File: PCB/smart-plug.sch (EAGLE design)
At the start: 15 parts, among them K1 HLS8L-DC3V-S-C, T1 2N2222, X3 OUT-3PINS

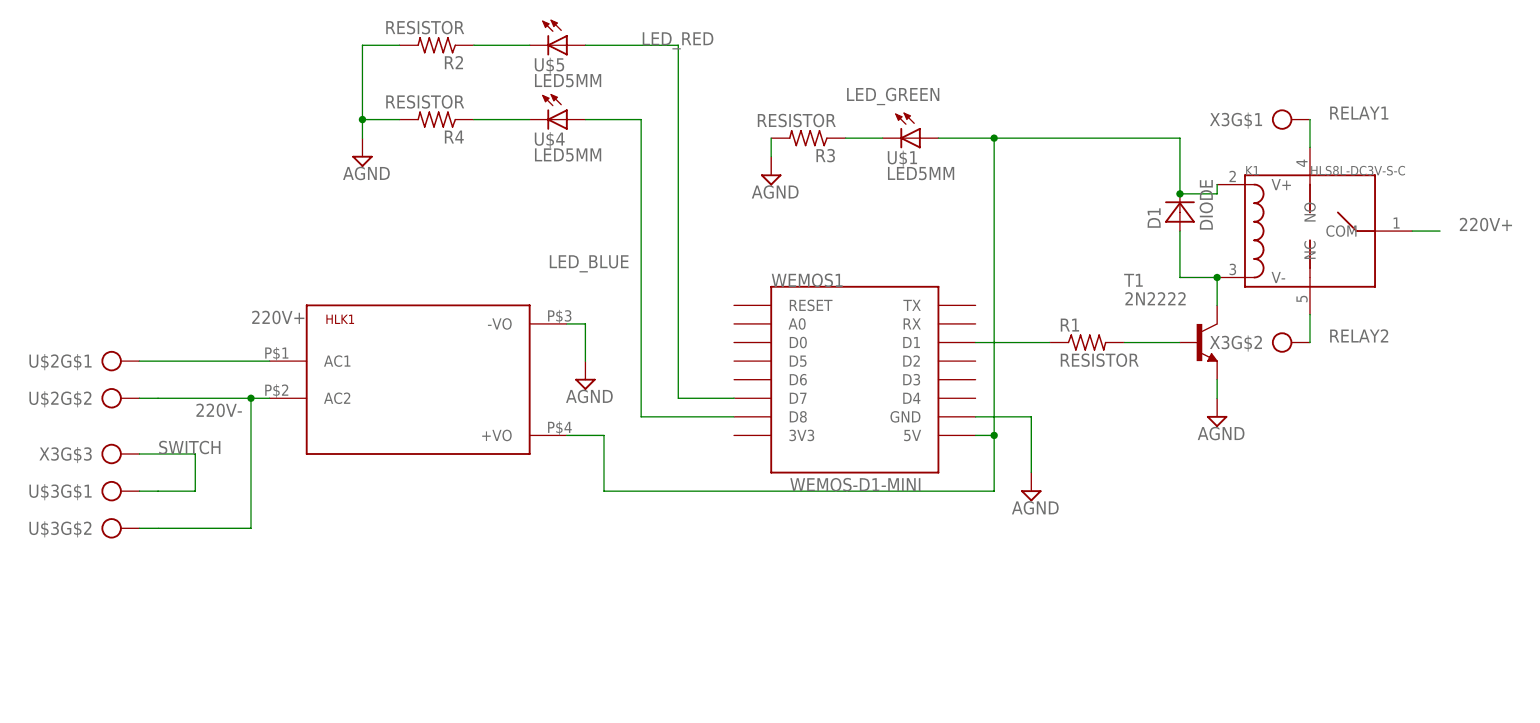
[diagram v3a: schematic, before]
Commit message: Update PCB files
Improved design, added SMD components and current sensor
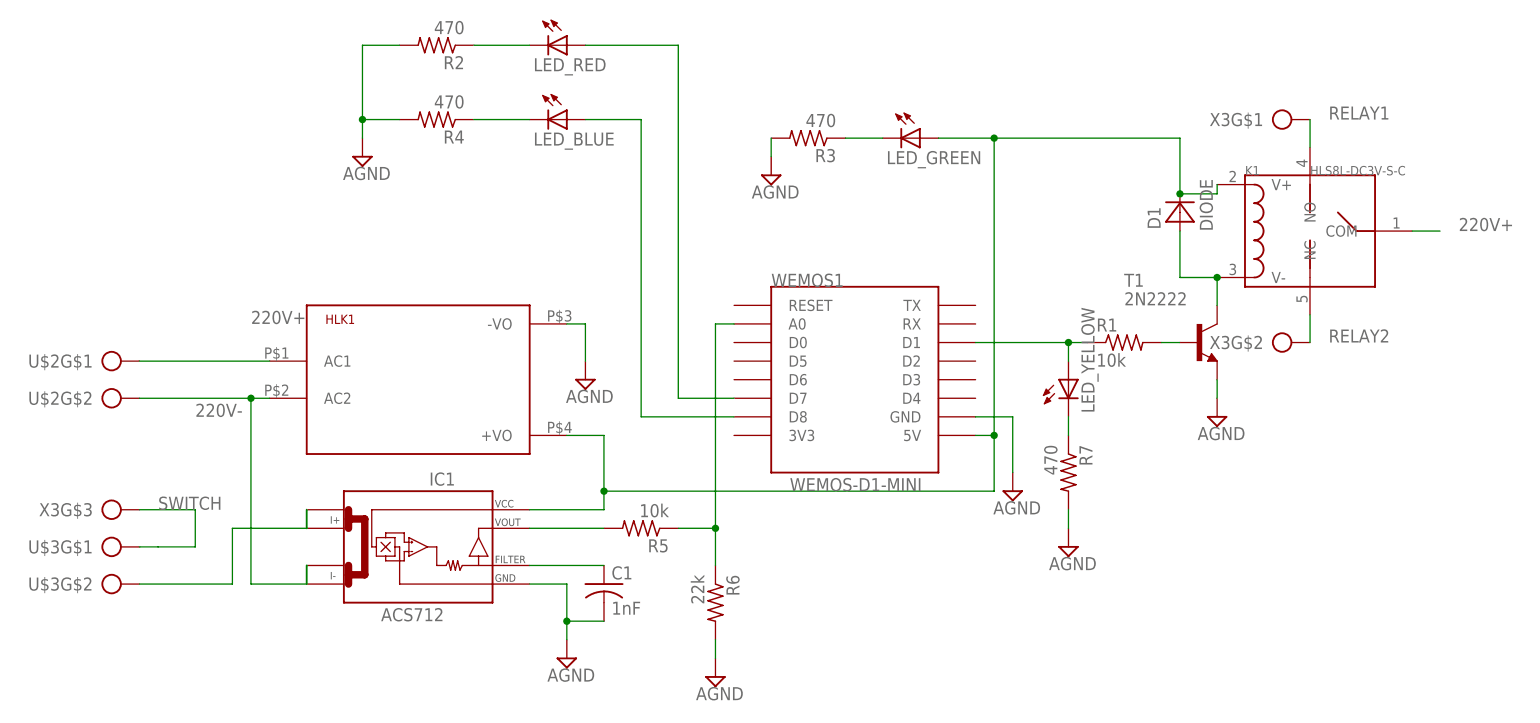
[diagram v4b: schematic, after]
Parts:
- removed U$1, U$4, U$5: LED5MM, smartplug-components:LED5MM
- added C1: 1nF, adafruit:C-USC1206
- added IC1: ACS712, ACS712:ACS712
- added LED_BLUE, LED_GREEN, LED_RED, LED_YELLOW: (no value), adafruit:LEDCHIP-LED0805
- added R5: 10k, adafruit:R-US_R1206
- added R6: 22k, adafruit:R-US_R1206
- added R7: 470, adafruit:R-US_R1206
- R1: value RESISTOR -> 10k; device smartplug-components:RESISTOR -> adafruit:R-US_R1206
- R2, R3, R4: value RESISTOR -> 470; device smartplug-components:RESISTOR -> adafruit:R-US_R1206
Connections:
- new net LED_GREEN1: LED_YELLOW.C, R7.1
- new net N$1: IC1.I+_1, U$3G$2.KL
- new net N$5: C1.1, IC1.FILTER
- new net N$7: IC1.VOUT, R5.2
- new net N$8: R5.1, R6.1, WEMOS1.A0
- net 220V-: now also IC1.I-_1; no longer U$3G$2.KL
- net AGND: now also C1.2, IC1.GND, R6.2, R7.2
- net LED_BLUE: now also LED_BLUE.A; no longer U$4.A
- net LED_GREEN: now also LED_GREEN.C; no longer U$1.C
- net LED_RED: now also LED_RED.A; no longer U$5.A
- net N$10: now also LED_BLUE.C; no longer U$4.C
- net N$2: now also LED_YELLOW.A
- net N$4: now also IC1.VCC, LED_GREEN.A; no longer U$1.A
- net N$9: now also LED_RED.C; no longer U$5.C
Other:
- moved on the sheet: R1, U$3G$1, U$3G$2, X3G$3
